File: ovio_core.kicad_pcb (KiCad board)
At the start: 6 copper layers, 98 x 27.5 mm, 189 parts, among them J101 Conn_01x06, J301 Conn_01x06, J701 USB3_B_Micro, Q501 NTZD3155C, U101 IP4254CZ8-4-TTL, U102 ECP5U_85_CABGA381, U201 TLV62569DRL, U202 TLV62569DRL, U203 TLV62569DRL, U204 TLV62569DRL, U301 IP4254CZ8-4-TTL, U302 W25Q128JVP, U401 MT9V034, U402 MT9V034, U403 KC2520Z, U501 ISM330DHC, U601 MT41J128M16JT-125:K, U701 FT600Q, Y701 30 MHz

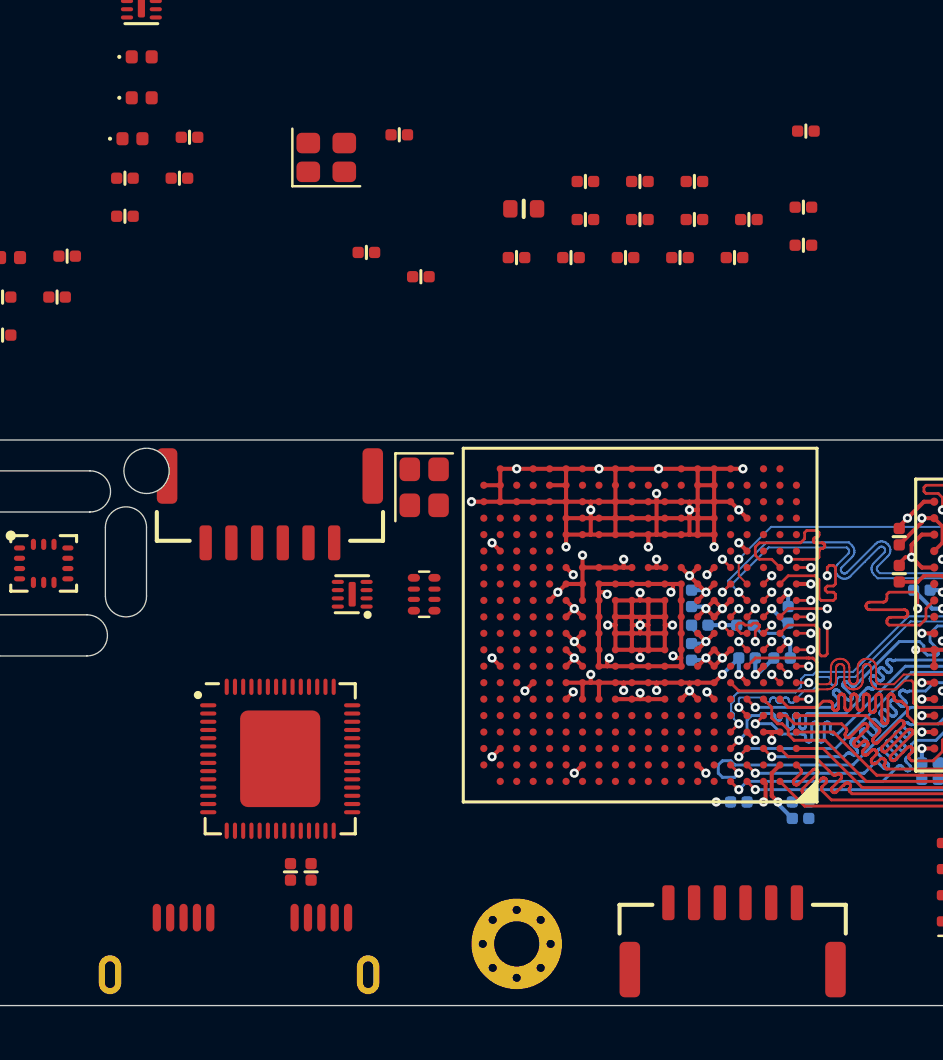
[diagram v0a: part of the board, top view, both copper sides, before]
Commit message: USB 3.0 chip layout
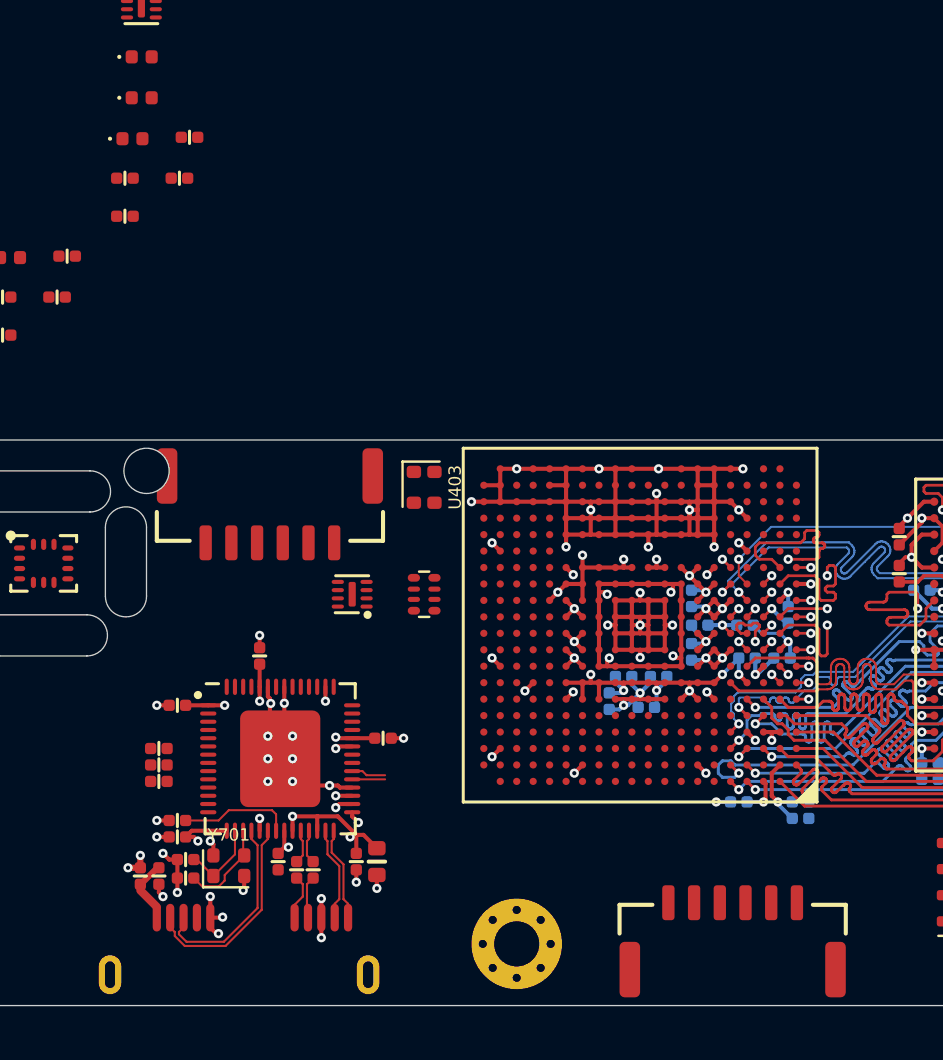
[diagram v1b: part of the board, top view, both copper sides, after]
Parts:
- C701, C702, C703, C704: moved to B.Cu
- C710, C711: value ~ -> 11p
- U403: value KC2520Z -> KC2016Z50.0000C15XXK; footprint crystals:Crystal_SMD_2520-4Pin_2.5x2.0mm -> crystals:Crystal_4Pin_2.0x1.6mm
- Y701: footprint crystals:Crystal_SMD_2520-4Pin_2.5x2.0mm -> crystals:Crystal_4Pin_2.0x1.6mm
- moved C706 46.0 mm to (180.5, 106.8), turned to 180 degrees
- moved FB701 45.8 mm to (178.7, 108.7), turned to 270 degrees
- moved C710 41.2 mm to (180.9, 107.9), turned to 180 degrees
- moved R701 40.8 mm to (179.6, 104.1)
- moved C711 40.5 mm to (180.9, 108.8), turned to 180 degrees
- moved C715 36.6 mm to (189.2, 108.0), turned to 270 degrees
- moved C714 35.3 mm to (185.4, 108.0), turned to 270 degrees
- moved R702 35.1 mm to (179.6, 103.3)
- moved Y701 34.8 mm to (183.0, 108.2)
- moved C709 32.6 mm to (180.5, 100.4), turned to 180 degrees
- moved C716 32.5 mm to (190.2, 108.0), turned to 270 degrees
- moved R703 32.0 mm to (179.6, 102.5)
- moved C705 31.8 mm to (179.6, 108.7), turned to 270 degrees
- moved R704 29.1 mm to (180.5, 106.0), turned to 180 degrees
- moved C708 29.0 mm to (190.5, 102.0)
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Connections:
- net Net-(C712-Pad2) renamed /USB Interface/TX_P_N
- net Net-(C713-Pad2) renamed /USB Interface/TX_P_P
- Y701 pad 1: Net-(C711-Pad1) -> Net-(C710-Pad1)
- Y701 pad 3: Net-(C710-Pad1) -> Net-(C711-Pad1)
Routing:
- net GND: track 182.0 -> 210.3 mm, vias 58 -> 84
- net +3V3: track 7.29 -> 22.0 mm, vias 4 -> 12
- net VD10: track 0.00 -> 10.9 mm, vias 0 -> 5
- net /USB Interface/D_N: track 0.00 -> 10.1 mm
- net /USB Interface/D_P: track 0.00 -> 9.44 mm
- net /USB Interface/FT_REF: track 0.00 -> 5.49 mm
- net Net-(C711-Pad1): track 0.00 -> 4.62 mm
- net /USB Interface/RX_P: track 0.00 -> 4.60 mm
- net /USB Interface/RX_N: track 0.00 -> 4.60 mm
- net Net-(C710-Pad1): track 0.00 -> 3.92 mm
- net /USB Interface/VBUS_IN: track 0.00 -> 3.19 mm
- net /USB Interface/TX_N: track 0.00 -> 2.21 mm
- net /USB Interface/TX_P: track 0.00 -> 2.07 mm
- net +5V: track 0.00 -> 1.82 mm, vias 0 -> 3
- net /USB Interface/FT_D1: track 0.00 -> 1.68 mm
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
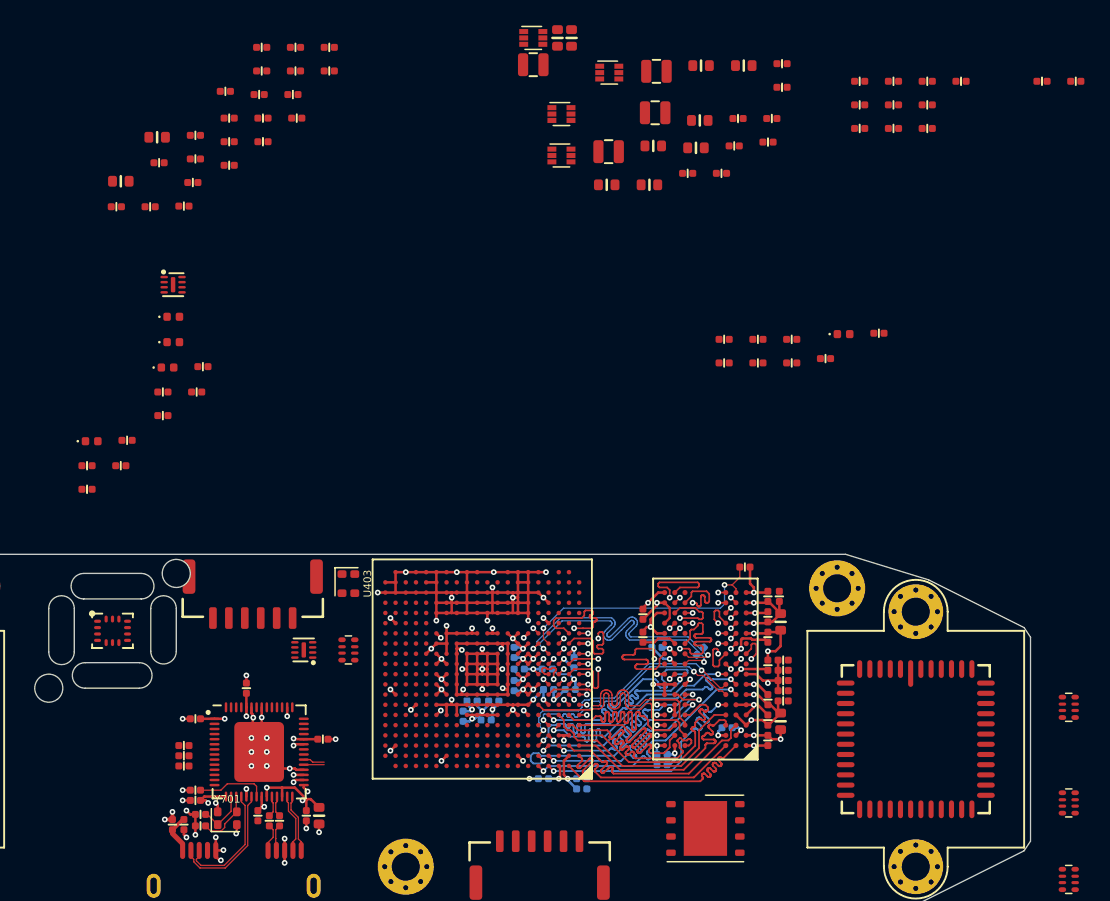
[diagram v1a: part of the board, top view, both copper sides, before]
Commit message: USB fifo routed
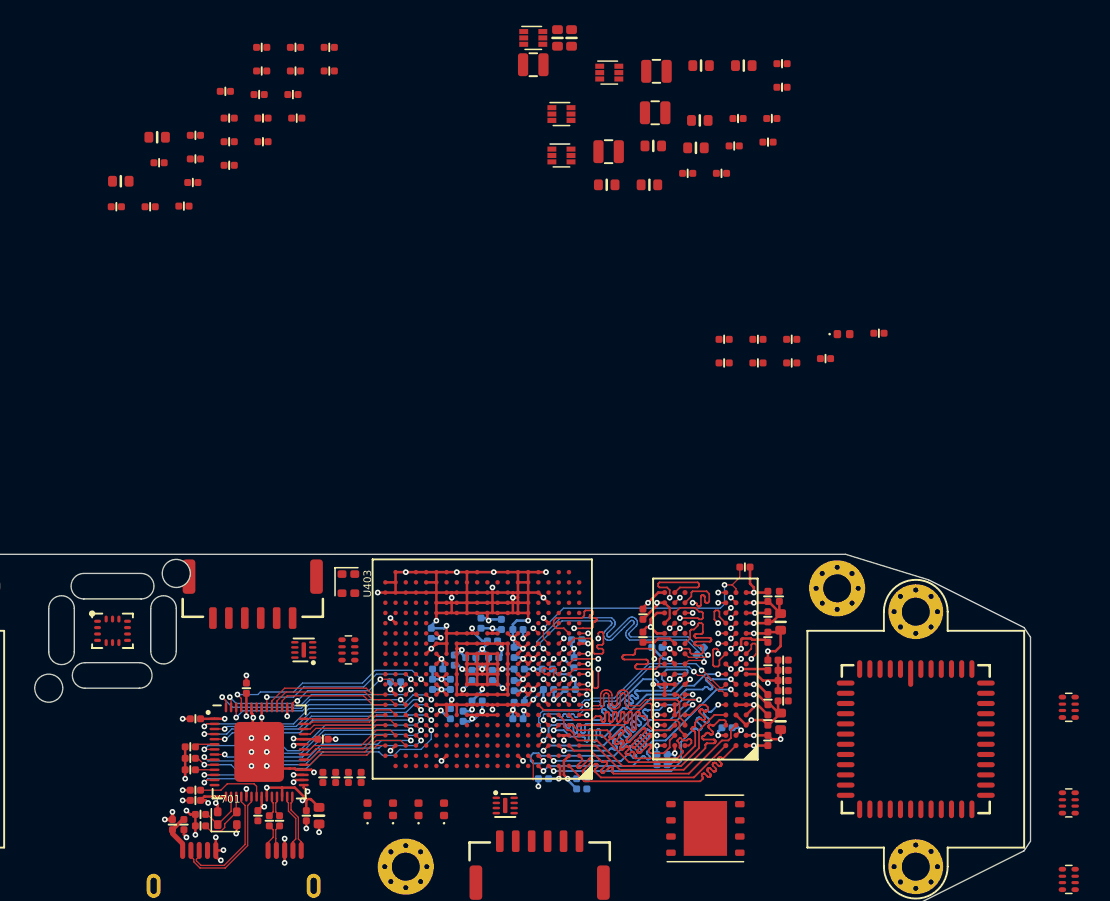
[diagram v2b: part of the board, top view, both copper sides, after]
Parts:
- C101, C102, C103, C104, C210, C211, C212, C213, C214, C215, C216, C217, C218, C219, C627, C628: moved to B.Cu
- moved C627 63.7 mm to (205.9, 99.1), turned to 180 degrees
- moved C218 59.3 mm to (203.8, 97.0), turned to 90 degrees
- moved C628 58.7 mm to (210.4, 94.2), turned to 180 degrees
- moved C211 57.5 mm to (200.5, 100.0), turned to 90 degrees
- moved C217 56.8 mm to (199.0, 93.7), turned to 90 degrees
- moved C219 55.8 mm to (200.8, 95.8), turned to 270 degrees
- moved C212 55.0 mm to (203.9, 95.6), turned to 180 degrees
- moved C210 54.5 mm to (202.1, 95.6)
- moved C216 54.2 mm to (202.2, 97.0), turned to 90 degrees
- moved C215 53.7 mm to (205.8, 93.4), turned to 180 degrees
- moved C213 53.5 mm to (205.8, 100.4), turned to 180 degrees
- moved C214 52.5 mm to (203.8, 94.3), turned to 180 degrees
- moved U101 48.4 mm to (204.8, 107.2)
- moved D101 44.1 mm to (200.0, 107.5), turned to 90 degrees
- moved D102 41.4 mm to (198.0, 107.5), turned to 90 degrees
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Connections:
- R702 pad 2: /~FT_RESET -> /USB Interface/~FT_RESET
- U102 pad A10: /USB Interface/FT_CLKOUT -> /2x cameras/CAM0_PIXCLK
- U102 pad A11: /USB Interface/FT_D13 -> Net-(U102-PadA11)
- U102 pad A15: /IMU_INT -> Net-(U102-PadA15)
- U102 pad A16: /P_USER_GPIO1 -> /P_USER_GPIO0
- U102 pad A17: /LED4 -> /LED3
- U102 pad A6: /USB Interface/FT_BE0 -> /2x cameras/CAM0_FLASH
- U102 pad A7: /USB Interface/FT_D5 -> /2x cameras/CAM0_D9
- U102 pad A8: /USB Interface/FT_D6 -> /2x cameras/CAM0_TRIGGER
- U102 pad A9: /USB Interface/FT_D11 -> Net-(U102-PadA9)
- U102 pad B10: /USB Interface/FT_D12 -> Net-(U102-PadB10)
- U102 pad B11: /USB Interface/FT_D14 -> Net-(U102-PadB11)
- U102 pad B12: /~FT_RESET -> Net-(U102-PadB12)
- U102 pad B15: /IMU_HEATER -> /IMU_INT
- U102 pad B16: /P_USER_GPIO2 -> /P_USER_GPIO1
- U102 pad B17: /LED2 -> /LED1
- U102 pad B18: Net-(U102-PadB18) -> /LED4
- U102 pad B6: /USB Interface/FT_BE1 -> /2x cameras/CAM0_FV_P
- U102 pad B8: /USB Interface/FT_D4 -> /2x cameras/CAM0_D8
- U102 pad B9: /USB Interface/FT_D9 -> Net-(U102-PadB9)
- U102 pad C10: /USB Interface/FT_D10 -> Net-(U102-PadC10)
- U102 pad C11: /USB Interface/FT_D15 -> Net-(U102-PadC11)
- U102 pad C15: Net-(U102-PadC15) -> /IMU_HEATER
- U102 pad C16: Net-(U102-PadC16) -> /P_USER_GPIO2
- U102 pad C17: /LED3 -> /LED2
- U102 pad C18: /2x cameras/CAM0_FLASH -> /USB Interface/FT_D1
- U102 pad C20: Net-(U102-PadC20) -> /USB Interface/FT_D0
- U102 pad C6: /USB Interface/~FT_OE -> /2x cameras/CAM0_D3
- U102 pad C7: /USB Interface/FT_D0 -> /2x cameras/CAM0_D4
- U102 pad C8: /USB Interface/FT_D3 -> /2x cameras/CAM0_D7
- U102 pad D11: /FT_GPIO0 -> Net-(U102-PadD11)
- U102 pad D15: /P_USER_FLASH_OUT -> Net-(U102-PadD15)
- U102 pad D16: /LED1 -> Net-(U102-PadD16)
- U102 pad D17: /2x cameras/CAM0_FV_P -> /USB Interface/FT_GPIO0
- U102 pad D18: /2x cameras/CAM0_D1 -> /USB Interface/~FT_RESET
- U102 pad D19: Net-(U102-PadD19) -> /USB Interface/FT_D3
- U102 pad D20: Net-(U102-PadD20) -> /USB Interface/FT_D2
- U102 pad D6: /USB Interface/~FT_RXF -> /2x cameras/CAM0_D0
- U102 pad D7: /USB Interface/~FT_RD -> /2x cameras/CAM0_D2
- U102 pad D8: /USB Interface/FT_D2 -> /2x cameras/CAM0_D6
- U102 pad D9: /USB Interface/FT_D7 -> /2x cameras/CAM0_SYSCLK
- U102 pad E11: /FT_GPIO1 -> Net-(U102-PadE11)
- U102 pad E15: /P_USER_GPIO0 -> /P_USER_FLASH_OUT
- U102 pad E16: /2x cameras/CAM0_LV_P -> /USB Interface/FT_GPIO1
- U102 pad E17: /2x cameras/CAM0_D2 -> /USB Interface/~FT_OE
- U102 pad E18: /2x cameras/CAM0_D3 -> /USB Interface/~FT_RD
- U102 pad E19: Net-(U102-PadE19) -> /USB Interface/FT_D5
- U102 pad E20: Net-(U102-PadE20) -> /USB Interface/FT_D4
- U102 pad E6: /USB Interface/~FT_TXE -> /2x cameras/CAM0_LV_P
- U102 pad E7: /USB Interface/~FT_WR -> /2x cameras/CAM0_D1
- U102 pad E8: /USB Interface/FT_D1 -> /2x cameras/CAM0_D5
- U102 pad E9: /USB Interface/FT_D8 -> Net-(U102-PadE9)
- U102 pad F16: /2x cameras/CAM0_D0 -> /USB Interface/~FT_TXE
- U102 pad F17: /2x cameras/CAM0_D5 -> /USB Interface/~FT_WR
- U102 pad F18: /2x cameras/CAM0_D4 -> /USB Interface/~FT_RXF
- U102 pad F19: Net-(U102-PadF19) -> /USB Interface/FT_D7
- U102 pad F20: Net-(U102-PadF20) -> /USB Interface/FT_D6
- U102 pad G16: /2x cameras/CAM0_D7 -> /USB Interface/FT_BE1
- U102 pad G18: /2x cameras/CAM0_D6 -> /USB Interface/FT_D15
- U102 pad G19: Net-(U102-PadG19) -> /USB Interface/FT_D9
- U102 pad G20: Net-(U102-PadG20) -> /USB Interface/FT_D8
- U102 pad H16: /2x cameras/CAM0_D8 -> /USB Interface/FT_D13
- U102 pad H17: /2x cameras/CAM0_TRIGGER -> /USB Interface/FT_BE0
- U102 pad H18: /2x cameras/CAM0_D9 -> /USB Interface/FT_D14
- U102 pad H20: Net-(U102-PadH20) -> /USB Interface/FT_D10
- U102 pad J16: Net-(U102-PadJ16) -> /USB Interface/FT_D12
- U102 pad J17: /2x cameras/CAM0_SYSCLK -> /USB Interface/FT_D11
- U102 pad J18: Net-(U102-PadJ18) -> +3V3
- U102 pad J19: /2x cameras/CAM0_PIXCLK -> /USB Interface/FT_CLKOUT
- U701 pad 10: /~FT_RESET -> /USB Interface/~FT_RESET
- U701 pad 12: /FT_GPIO0 -> /USB Interface/FT_GPIO0
- U701 pad 13: /FT_GPIO1 -> /USB Interface/FT_GPIO1
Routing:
- net GND: track 210.3 -> 234.8 mm
- net /USB Interface/FT_GPIO1: track 0.00 -> 21.6 mm, vias 0 -> 2
- net /USB Interface/~FT_TXE: track 0.00 -> 20.0 mm, vias 0 -> 2
- net /USB Interface/~FT_RESET: track 0.00 -> 19.7 mm, vias 0 -> 2
- net /USB Interface/~FT_WR: track 0.00 -> 19.6 mm, vias 0 -> 2
- net /USB Interface/~FT_OE: track 0.00 -> 19.6 mm, vias 0 -> 2
- net /USB Interface/FT_GPIO0: track 0.00 -> 19.5 mm, vias 0 -> 2
- net /USB Interface/FT_BE0: track 0.00 -> 19.3 mm, vias 0 -> 2
- net /USB Interface/FT_BE1: track 0.00 -> 18.5 mm, vias 0 -> 2
- net /USB Interface/FT_D13: track 0.00 -> 17.6 mm, vias 0 -> 2
- net /USB Interface/FT_D12: track 0.00 -> 17.2 mm, vias 0 -> 2
- net /USB Interface/~FT_RD: track 0.00 -> 16.9 mm, vias 0 -> 2
- net /USB Interface/~FT_RXF: track 0.00 -> 16.6 mm, vias 0 -> 2
- net /USB Interface/FT_D14: track 0.00 -> 16.4 mm, vias 0 -> 2
- net /USB Interface/FT_D15: track 0.00 -> 16.1 mm, vias 0 -> 2
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
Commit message: More routing
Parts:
- removed C417: 10n, passive:C_0402
- removed C419: 0.1u, passive:C_0402
- removed U301: IP4254CZ8-4-TTL, dfn:UDFN-8-1EP_1.7x1.35mm_P0.4mm_EP0.4x1.2mm
- added C220: 22u, passive:C_0603, F.Cu at (217.1, 50.7)
- added C303: 0.1u, passive:C_0402, F.Cu at (192.3, 92.8)
- added D501: LED_Small, LED_SMD:LED_0402_1005Metric, F.Cu at (226.5, 113.4)
- added R307: 10k, passive:R_0402, F.Cu at (184.7, 92.9)
- added R513: 1k, passive:R_0402, F.Cu at (229.3, 113.3)
- C412, C413, C414, C415, C416, C418: moved to B.Cu
- J301: footprint connectors:SM06B-GHS-TB -> Connector:Tag-Connect_TC2030-IDC-NL_2x03_P1.27mm_Vertical
- U201, U202, U203, U204: footprint Package_TO_SOT_SMD:SOT-563 -> sot:SOT-563
- moved RN401 92.6 mm to (246.0, 115.0)
- moved C409 91.4 mm to (128.3, 98.8)
- moved C410 91.4 mm to (130.9, 95.3)
- moved R402 91.4 mm to (130.9, 97.2)
- moved R404 91.4 mm to (131.2, 93.5)
- moved R410 91.4 mm to (131.2, 91.6)
- moved C401 90.7 mm to (252.5, 105.8)
- moved C404 90.7 mm to (251.9, 111.2)
- moved C408 90.7 mm to (266.0, 98.7)
- moved FB401 90.7 mm to (254.6, 111.2)
- moved R401 90.7 mm to (263.4, 104.3)
- moved R403 90.7 mm to (260.7, 98.7)
- moved R405 90.7 mm to (260.5, 102.4)
- moved C403 86.0 mm to (253.5, 102.0)
- moved C407 84.8 mm to (256.0, 98.5)
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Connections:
- net Net-(R201-Pad1) renamed /System Power/FB_1V1
- net Net-(R203-Pad1) renamed /System Power/FB_1V5
- net Net-(R205-Pad1) renamed /System Power/FB_2V5
- net Net-(R207-Pad1) renamed /System Power/FB_3V3
- C401 pad 1: /2x cameras/VAA -> /2x cameras/CAM0_VAA
- C402 pad 1: /2x cameras/VAA -> /2x cameras/CAM1_VAA
- C404 pad 1: /2x cameras/VAA -> /2x cameras/CAM0_VAA
- C406 pad 1: /2x cameras/VAA -> /2x cameras/CAM1_VAA
- C408 pad 1: /2x cameras/VAA -> /2x cameras/CAM0_VAA
- C410 pad 1: /2x cameras/VAA -> /2x cameras/CAM1_VAA
- FB401 pad 1: /2x cameras/VAA -> /2x cameras/CAM0_VAA
- FB402 pad 1: /2x cameras/VAA -> /2x cameras/CAM1_VAA
- J301 pad 1: +5V -> +3V3
- J301 pad 2: /FPGA Config/TCK -> /FPGA Config/TMS
- J301 pad 4: /FPGA Config/TDO -> /FPGA Config/TCK
- J301 pad 5: /FPGA Config/TMS -> GND
- J301 pad 6: GND -> /FPGA Config/TDO
- R401 pad 1: /CAM0_SDATA -> /2x cameras/CAM0_SDATA
- R402 pad 1: /CAM1_SDATA -> /2x cameras/CAM1_SDATA
- R403 pad 1: /CAM0_RESET -> /2x cameras/CAM0_RESET
- R404 pad 1: /CAM1_RESET -> /2x cameras/CAM1_RESET
- R405 pad 1: /CAM0_SCLK -> /2x cameras/CAM0_SCLK
- R406 pad 1: /CAM1_SCLK -> /2x cameras/CAM1_SCLK
- RN405 pad 1: /2x cameras/CAM0_PIXCLK_P -> /2x cameras/CAM0_SYSCLK_P
- RN405 pad 3: /2x cameras/CAM1_PIXCLK_P -> /2x cameras/CAM1_SYSCLK_P
- RN405 pad 6: /2x cameras/CAM1_PIXCLK -> /2x cameras/CAM1_SYSCLK
- RN405 pad 8: /2x cameras/CAM0_PIXCLK -> /2x cameras/CAM0_SYSCLK
- U101 pad 1: /P_USER_FLASH_OUT -> /P_USER_GPIO2
- U101 pad 2: /P_USER_GPIO0 -> /P_USER_GPIO1
- U101 pad 3: /P_USER_GPIO1 -> /P_USER_GPIO0
- U101 pad 4: /P_USER_GPIO2 -> /P_USER_FLASH_OUT
- U101 pad 5: /USER_GPIO2 -> /USER_FLASH_OUT
- U101 pad 6: /USER_GPIO1 -> /USER_GPIO0
- U101 pad 7: /USER_GPIO0 -> /USER_GPIO1
- U101 pad 8: /USER_FLASH_OUT -> /USER_GPIO2
- U102 pad A12: /CAM1_RESET -> Net-(U102-PadA12)
- U102 pad B13: /CAM0_SDATA -> Net-(U102-PadB13)
- U102 pad B9: Net-(U102-PadB9) -> /2x cameras/CAM0_SDATA
- U102 pad C10: Net-(U102-PadC10) -> /2x cameras/CAM0_SCLK
- U102 pad C13: /CAM0_SCLK -> Net-(U102-PadC13)
- U102 pad D12: /CAM1_SDATA -> Net-(U102-PadD12)
- U102 pad D13: /CAM0_RESET -> Net-(U102-PadD13)
- U102 pad E12: /CAM1_SCLK -> Net-(U102-PadE12)
- U102 pad E9: Net-(U102-PadE9) -> /2x cameras/CAM0_RESET
- U102 pad N19: Net-(U102-PadN19) -> /2x cameras/CAM1_SDATA
- U102 pad N20: Net-(U102-PadN20) -> /2x cameras/CAM1_SCLK
- U102 pad P19: Net-(U102-PadP19) -> /2x cameras/CAM1_RESET
- U102 pad R5: /FPGA Config/TDI_P -> /FPGA Config/TDI
- U102 pad T5: /FPGA Config/TCK_P -> /FPGA Config/TCK
- U102 pad U5: /FPGA Config/TMS_P -> /FPGA Config/TMS
- U102 pad V4: /FPGA Config/TDO_P -> /FPGA Config/TDO
- U401 pad 24: /CAM0_SDATA -> /2x cameras/CAM0_SDATA
- U401 pad 25: /CAM0_SCLK -> /2x cameras/CAM0_SCLK
- U401 pad 32: /CAM0_RESET -> /2x cameras/CAM0_RESET
- U401 pad 35: /2x cameras/VAA -> /2x cameras/CAM0_VAA
- U401 pad 39: /2x cameras/VAA -> /2x cameras/CAM0_VAA
- U401 pad 40: /2x cameras/VAA -> /2x cameras/CAM0_VAA
- U402 pad 24: /CAM1_SDATA -> /2x cameras/CAM1_SDATA
- U402 pad 25: /CAM1_SCLK -> /2x cameras/CAM1_SCLK
- U402 pad 32: /CAM1_RESET -> /2x cameras/CAM1_RESET
- U402 pad 35: /2x cameras/VAA -> /2x cameras/CAM1_VAA
- U402 pad 39: /2x cameras/VAA -> /2x cameras/CAM1_VAA
- U402 pad 40: /2x cameras/VAA -> /2x cameras/CAM1_VAA
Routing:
- net /DDR3 Memory/DRAM_VDD: track 18.7 -> 66.3 mm
- net /DDR3 Memory/DRAM_VDDQ: track 17.6 -> 43.1 mm
- net +3V3: track 27.9 -> 40.0 mm, vias 14 -> 18
- net /2x cameras/50MHZ_PLL_IN: track 0.00 -> 4.37 mm
- net /2x cameras/CAM0_FV_P: track 2.07 -> 0.00 mm
- net /FPGA Config/SPI_CS: track 0.00 -> 1.14 mm
- net GND: track 234.8 -> 235.8 mm, vias 84 -> 85
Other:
- outline, holes or cut-outs redrawn
